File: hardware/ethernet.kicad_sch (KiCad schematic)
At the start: 69 parts, among them Q1 BSS138, Q2 BSS138, U14 KSZ9031RNXCA, U4 CCGM1A1, X1 ECS-2520MV-250-xx

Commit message: Sorting ethernet
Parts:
- R68, R69, R74, R75, R76, R77, R80, R81, R82, R83: now left out of the parts list
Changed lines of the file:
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@@
 		(at 35.56 104.14 90)
 		(unit 1)
-		(exclude_from_sim no)
-		(in_bom yes)
-		(on_board yes)
+		(exclude_from_sim yes)
+		(in_bom no)
+		(on_board no)
 		(dnp no)
 		(property "Reference" "R68"
@@
 		(at 35.56 119.38 90)
 		(unit 1)
-		(exclude_from_sim no)
-		(in_bom yes)
-		(on_board yes)
+		(exclude_from_sim yes)
+		(in_bom no)
+		(on_board no)
 		(dnp no)
 		(property "Reference" "R74"
@@
 		(at 71.12 111.76 90)
 		(unit 1)
-		(exclude_from_sim no)
-		(in_bom yes)
-		(on_board yes)
+		(exclude_from_sim yes)
+		(in_bom no)
+		(on_board no)
 		(dnp no)
 		(property "Reference" "R81"
@@
 		(at 71.12 101.6 90)
 		(unit 1)
-		(exclude_from_sim no)
-		(in_bom yes)
-		(on_board yes)
+		(exclude_from_sim yes)
+		(in_bom no)
+		(on_board no)
 		(dnp no)
 		(property "Reference" "R77"
@@
 		(at 71.12 109.22 90)
 		(unit 1)
-		(exclude_from_sim no)
-		(in_bom yes)
-		(on_board yes)
+		(exclude_from_sim yes)
+		(in_bom no)
+		(on_board no)
 		(dnp no)
 		(property "Reference" "R80"
@@
 		(at 35.56 121.92 90)
 		(unit 1)
-		(exclude_from_sim no)
-		(in_bom yes)
-		(on_board yes)
+		(exclude_from_sim yes)
+		(in_bom no)
+		(on_board no)
 		(dnp no)
 		(property "Reference" "R75"
@@
 		(at 71.12 99.06 90)
 		(unit 1)
-		(exclude_from_sim no)
-		(in_bom yes)
-		(on_board yes)
+		(exclude_from_sim yes)
+		(in_bom no)
+		(on_board no)
 		(dnp no)
 		(property "Reference" "R76"
@@
 		(at 35.56 106.68 90)
 		(unit 1)
-		(exclude_from_sim no)
-		(in_bom yes)
-		(on_board yes)
+		(exclude_from_sim yes)
+		(in_bom no)
+		(on_board no)
 		(dnp no)
 		(property "Reference" "R69"
@@
 		(at 71.12 116.84 90)
 		(unit 1)
-		(exclude_from_sim no)
-		(in_bom yes)
-		(on_board yes)
+		(exclude_from_sim yes)
+		(in_bom no)
+		(on_board no)
 		(dnp no)
 		(property "Reference" "R83"
@@
 		(at 71.12 114.3 90)
 		(unit 1)
-		(exclude_from_sim no)
-		(in_bom yes)
-		(on_board yes)
+		(exclude_from_sim yes)
+		(in_bom no)
+		(on_board no)
 		(dnp no)
 		(property "Reference" "R82"

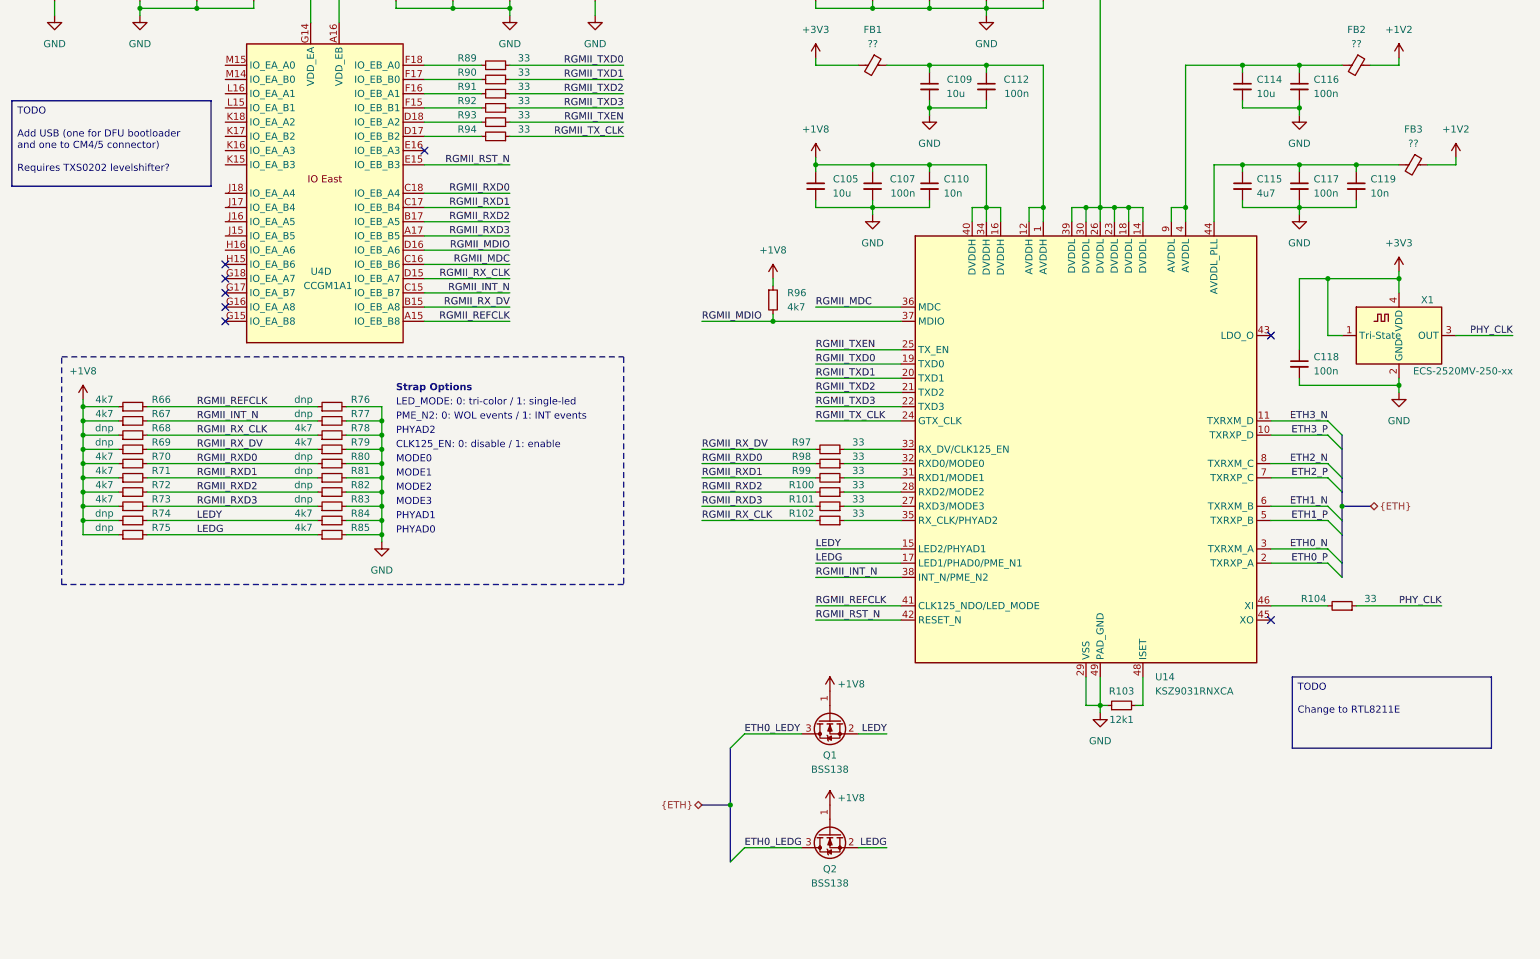
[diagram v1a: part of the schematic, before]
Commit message: Adding USB connector and level converter
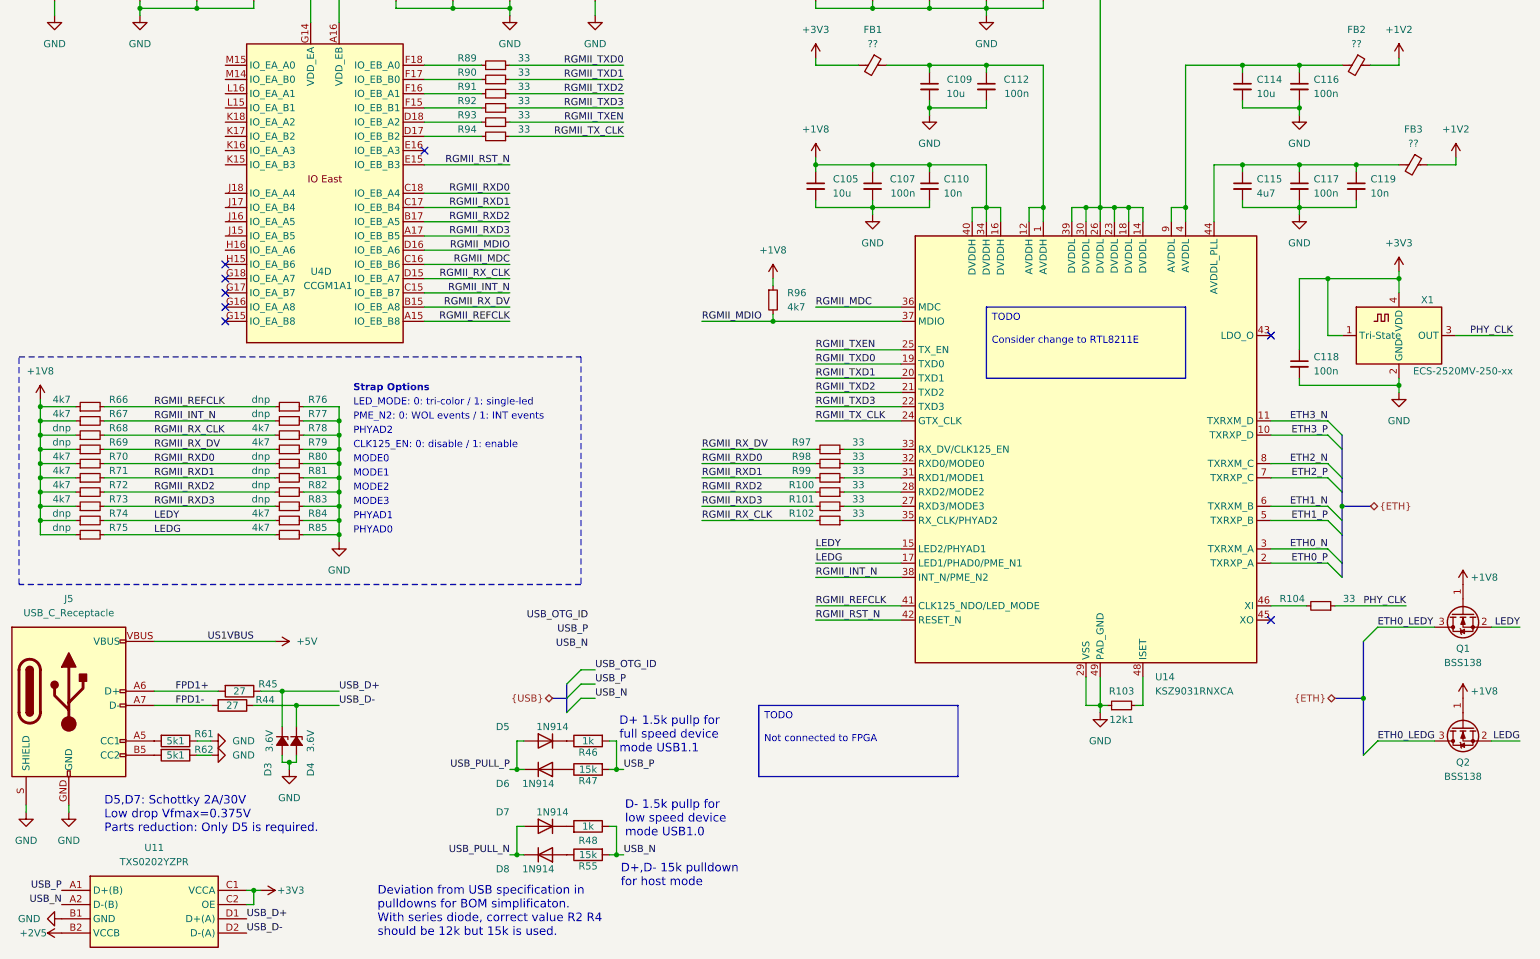
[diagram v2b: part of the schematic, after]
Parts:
- added D3, D4: 3.6V, Diode_SMD:D_SOD-323_HandSoldering, symbol USB-rescue:D_Zener_Small_ALT-Device
- added D5, D6, D7, D8: 1N914, Diode_SMD:D_SOD-323_HandSoldering, symbol Device:D
- added J5: USB_C_Receptacle, ulx5m-gs:USB-C_16, symbol SparkFun-Connector:USB_C_Receptacle
- added R44, R45: 27, Resistor_SMD:R_0402_1005Metric, symbol Device:R
- added R46, R48: 1k, Resistor_SMD:R_0402_1005Metric, symbol Device:R
- added R47, R55: 15k, Resistor_SMD:R_0402_1005Metric, symbol Device:R
- added R61, R62: 5k1, Resistor_SMD:R_0402_1005Metric, symbol Device:R
- added U11: TXS0202YZPR, TXS0202:BGA8C50P2X4_89X189X50, symbol TXS0202YZPR:TXS0202YZPR
- U4: footprint Package_BGA:BGA-324_15.0x15.0mm_Layout18x18_P0.8mm_Ball0.45mm_Pad0.4mm_NSMD -> ulx5m-gs:BGA-324_15.0x15.0mm_Layout18x18_P0.8mm_Ball0.45mm_Pad0.4mm_NSMD
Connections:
- net +3V3: now also U11.C1 (VCCA), U11.C2 (OE)
- net GND: now also D3.2 (A), D4.2 (A), J5.GND, J5.S (SHIELD), R61.1, R62.1, U11.B1 (GND)
- new net: D8.2 (A), R55.1
- new net: D7.1 (K), R48.2
- new net: J5.A5 (CC1), R61.2
- new net: J5.A8 (NC), J5.B8 (NC)
- new net: J5.B5 (CC2), R62.2
- new net: J5.NC1 (NC), J5.NC2 (NC), J5.NC3 (NC)
- new net: D6.2 (A), R47.1
- new net: D5.1 (K), R46.1
- new net +2V5: U11.B2 (VCCB)
- new net +5V: J5.VBUS
- new net FPD1+: J5.A6 (D+), J5.B6 (D+), R45.2
- new net FPD1-: J5.A7 (D-), J5.B7 (D-), R44.2
- new net USB_D+: D3.1 (K), R45.1, U11.D1 (D+(A))
- new net USB_D-: D4.1 (K), R44.1, U11.D2 (D-(A))
- new net USB_N: R48.1, R55.2, U11.A2 (D-(B))
- new net USB_P: R46.2, R47.2, U11.A1 (D+(B))
- new net USB_PULL_N: D7.2 (A), D8.1 (K)
- new net USB_PULL_P: D5.2 (A), D6.1 (K)
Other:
- note added: "D+ 1.5k pullp for full speed device mode USB1.1"
- note added: "D+,D- 15k pulldown for host mode"
- note added: "D- 1.5k pullp for low speed device mode USB1.0"
- note added: "D5,D7: Schottky 2A/30V Low drop Vfmax=0.375V Parts reduction: Only D5 is required."
- note added: "Deviation from USB specification in pulldowns for BOM simplificaton. With series diode, correct value R2 R4 should be 12k but 15k is used."
- moved on the sheet: Q1, Q2, R104, R66, R67, R68, R69, R70, R71, R72, R73, R74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

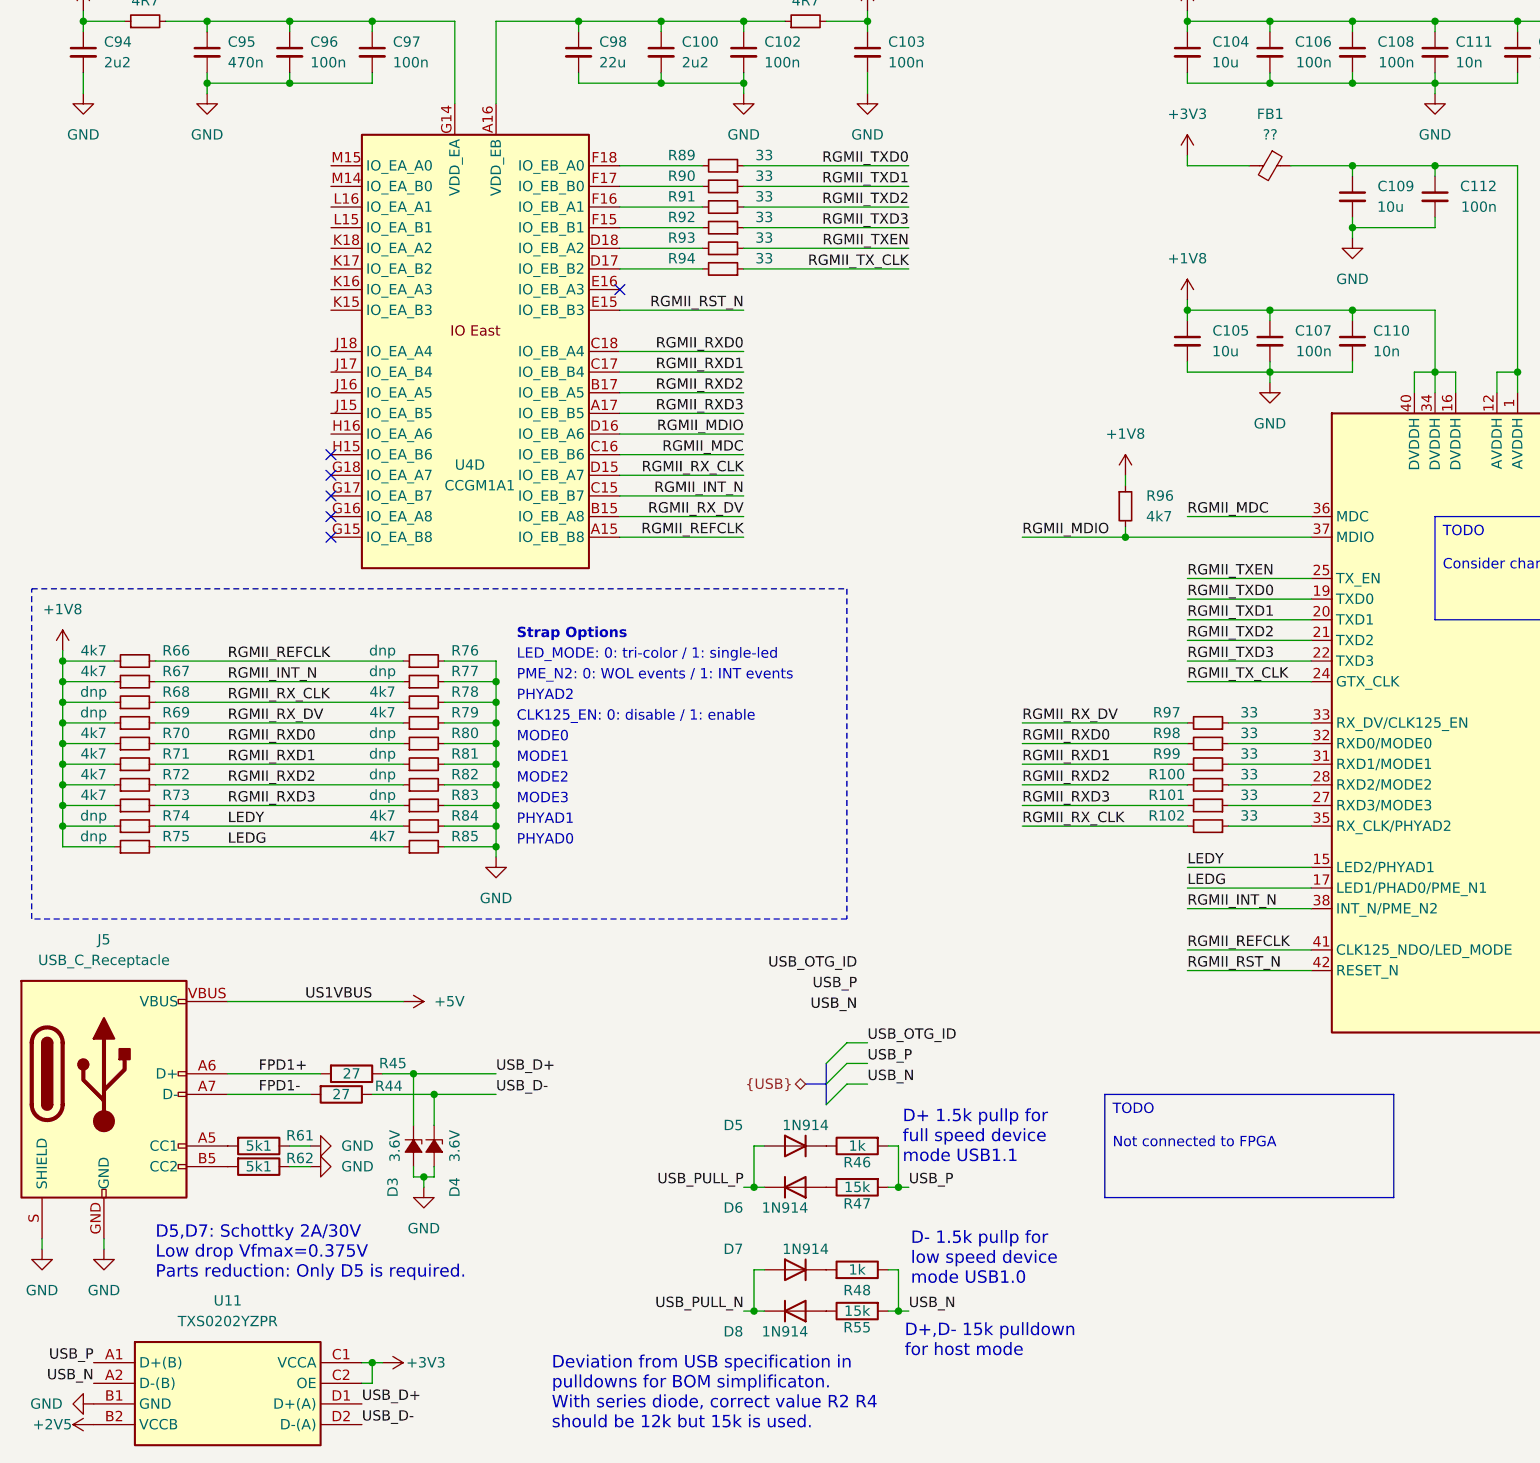
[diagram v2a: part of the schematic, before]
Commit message: Connecting USB
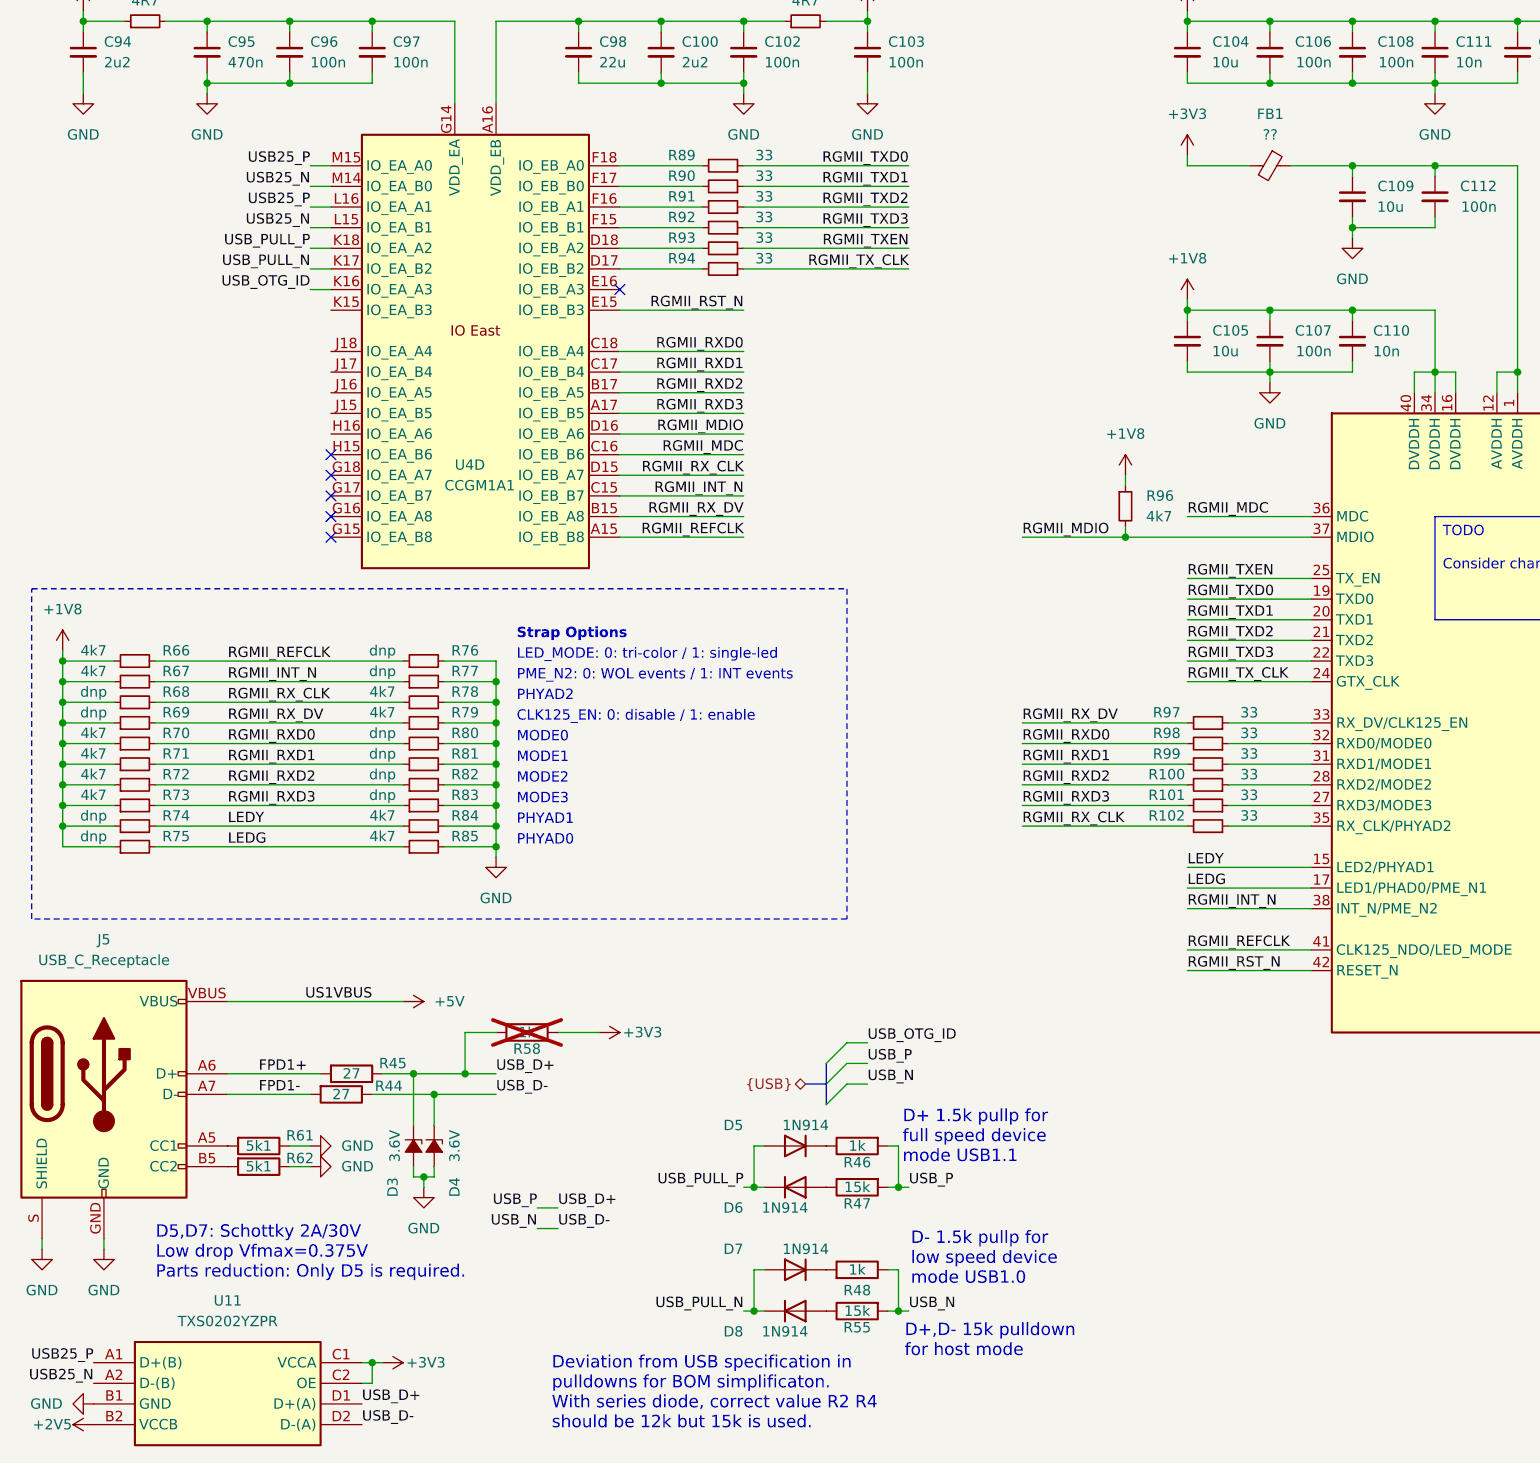
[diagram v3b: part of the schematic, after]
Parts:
- added R58: 1k, Resistor_SMD:R_0402_1005Metric, symbol Device:R
- D3, D4, D5, D6, D7, D8: footprint Diode_SMD:D_SOD-323_HandSoldering -> Diode_SMD:D_SOD-523
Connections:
- net +3V3: now also R58.2
- net USB_D+: now also R46.2, R47.2, R58.1
- net USB_D-: now also R48.1, R55.2
- net USB_OTG_ID: now also U4.K16 (IO_EA_A3)
- net USB_PULL_N: now also U4.K17 (IO_EA_B2)
- net USB_PULL_P: now also U4.K18 (IO_EA_A2)
- net USB25_N: now reaches U4.L15 (IO_EA_B1)
- net USB25_N: now also U11.A2 (D-(B)), U4.M14 (IO_EA_B0)
- net USB25_P: now reaches U4.L16 (IO_EA_A1)
- net USB25_P: now also U11.A1 (D+(B)), U4.M15 (IO_EA_A0)
- removed net USB_N: R48.1, R55.2, U11.A2 (D-(B))
- removed net USB_P: R46.2, R47.2, U11.A1 (D+(B))

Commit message: Routing diff clock
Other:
- company: (none) -> ${project_creator}
- title: (none) -> ${project_name}
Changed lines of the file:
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@@
 	(generator_version "9.0")
 	(paper "A4")
+	(title_block
+		(title "${project_name}")
+		(date "2025-06-24")
+		(rev "${project_version}")
+		(company "${project_creator}")
+		(comment 1 "${project_license}")
+	)
 	(rectangle
 		(start 15.24 90.17)

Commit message: Clearing errors
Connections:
- net VCC_EA: now reaches C95.1, C96.1, C97.1, R125.2, U4.G14 (VDD_EA), U4.H17 (VDD_EA), U4.J14 (VDD_EA), U4.L14 (VDD_EA), U4.L17 (VDD_EA)
- net VCC_EB: now reaches C100.1, C102.1, C98.1, R124.1, U4.A16 (VDD_EB), U4.B18 (VDD_EB), U4.E14 (VDD_EB), U4.E17 (VDD_EB), U4.F13 (VDD_EB)
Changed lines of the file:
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@@
 	(wire
 		(pts
+			(xy 113.03 20.32) (xy 118.11 20.32)
+		)
+		(stroke
+			(width 0)
+			(type default)
+		)
+	)
+	(wire
+		(pts
 			(xy 157.48 36.83) (xy 157.48 38.1)
 		)
@@
 	(wire
 		(pts
-			(xy 113.03 20.32) (xy 118.11 20.32)
-		)
-		(stroke
-			(width 0)
-			(type default)
-		)
-	)
-	(wire
-		(pts
 			(xy 157.48 129.54) (xy 172.72 129.54)
 		)
@@
 	(wire
 		(pts
-			(xy 31.75 20.32) (xy 36.83 20.32)
-		)
-		(stroke
-			(width 0)
-			(type default)
-		)
-	)
-	(wire
-		(pts
 			(xy 46.99 20.32) (xy 46.99 21.59)
 		)
@@
 	(wire
 		(pts
+			(xy 31.75 20.32) (xy 36.83 20.32)
+		)
+		(stroke
+			(width 0)
+			(type default)
+		)
+	)
+	(wire
+		(pts
 			(xy 82.55 27.94) (xy 92.71 27.94)
 		)
@@
 		)
 	)
+	(label "VCC_EA"
+		(at 36.83 20.32 0)
+		(effects
+			(font
+				(size 1.27 1.27)
+			)
+			(justify left bottom)
+		)
+	)
 	(label "USB25_N"
 		(at 49.53 45.72 180)
@@
 		(effects
 			(font
+				(size 1.27 1.27)
+			)
+			(justify left bottom)
+		)
+	)
+	(label "VCC_EB"
+		(at 82.55 20.32 0)
+		(effects
+			(font

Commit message: Updat to CM5
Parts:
- added BTN1, BTN2, BTN3: SW_Push, Switch_EVPAA:Switch_EVPAA, symbol Switch:SW_Push
- added C67, C68, C69, C70, C71, C72, C73, C74: 10n, Capacitor_SMD:C_0402_1005Metric, symbol Device:C_Small
- added R118: 300, Resistor_SMD:R_0402_1005Metric, symbol Device:R
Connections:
- net +3V3: now also R118.2
- new net: BTN1.1, BTN2.1, BTN3.1, R118.1
- new net BTN1: BTN1.2
- new net BTN2: BTN2.2
- new net BTN3: BTN3.2
- new net DDMI1_CLK_N: C74.1
- new net DDMI1_CLK_P: C73.1
- new net DDMI1_TX0_N: C68.1
- new net DDMI1_TX0_P: C67.1
- new net DDMI1_TX1_N: C70.1
- new net DDMI1_TX1_P: C69.1
- new net DDMI1_TX2_N: C72.1
- new net DDMI1_TX2_P: C71.1
